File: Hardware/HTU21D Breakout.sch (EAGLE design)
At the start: 13 parts, among them U1 HTU21D

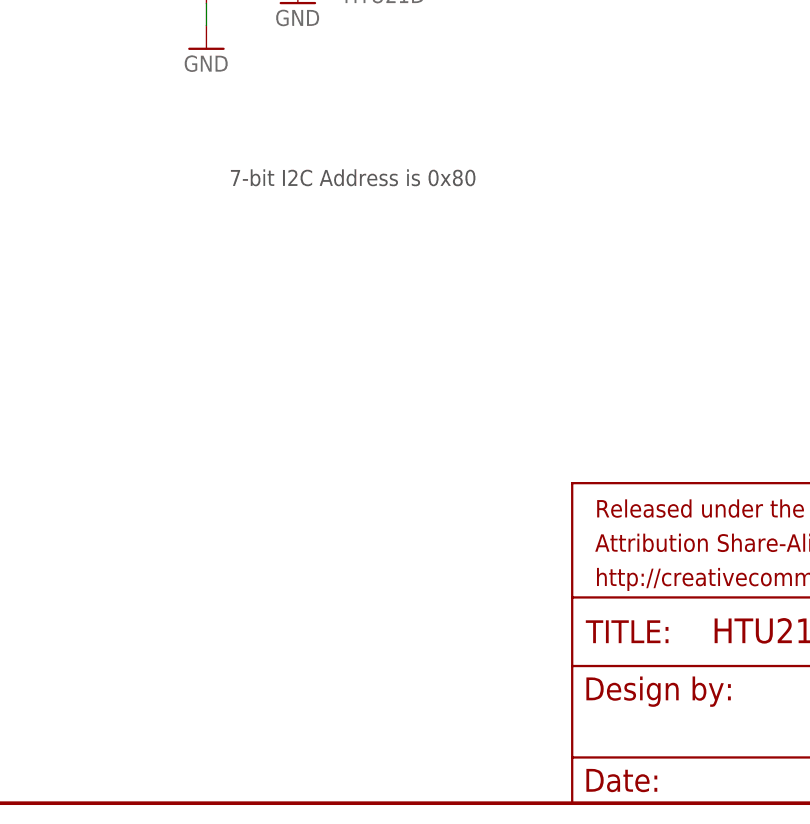
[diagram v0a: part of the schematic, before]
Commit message: Re-routing post review with engineering recommendations.
Moved to 0603 footprints. Removed ground planes to align with datasheet
thermal recommendations. Added OSHW logo. Updated frame to CC 3.0. Added
revision code to bottom copper.
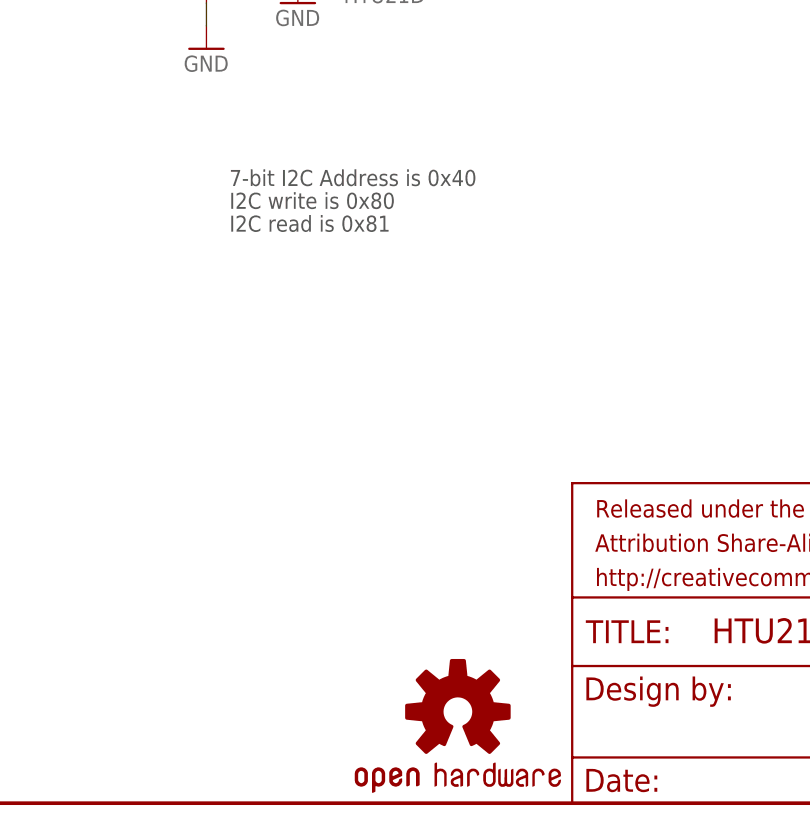
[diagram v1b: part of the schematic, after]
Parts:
- added LOGO2: OSHW-LOGOS, SparkFun-Aesthetics:OSHW-LOGOS
- C1: device SparkFun:CAP0402-CAP -> SparkFun:CAP0603-CAP
- R1, R2: device SparkFun:RESISTOR0402-RES -> SparkFun:RESISTOR0603-RES
- renumbered FRAME1 to FRAME2
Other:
- note added: "7-bit I2C Address is 0x40"
- note added: "I2C read is 0x81"
- note added: "I2C write is 0x80"
- note removed: "7-bit I2C Address is 0x80"
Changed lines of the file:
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@@
 <?xml version="1.0" encoding="utf-8"?>
 <!DOCTYPE eagle SYSTEM "eagle.dtd">
-<eagle version="6.5.0">
+<eagle version="6.4">
 <drawing>
 <settings>
@@
 </classes>
 <parts>
-<part name="FRAME1" library="SparkFun-Aesthetics" deviceset="FRAME-LETTER" device=""/>
 <part name="LOGO1" library="SparkFun" deviceset="LOGO-SFE" device="SK"/>
-<part name="C1" library="SparkFun" deviceset="CAP" device="0402-CAP" value="0.1uF"/>
-<part name="R1" library="SparkFun" deviceset="RESISTOR" device="0402-RES" value="4.7k"/>
-<part name="R2" library="SparkFun" deviceset="RESISTOR" device="0402-RES" value="4.7k"/>
+<part name="C1" library="SparkFun" deviceset="CAP" device="0603-CAP" value="0.1uF"/>
+<part name="R1" library="SparkFun" deviceset="RESISTOR" device="0603-RES" value="4.7k"/>
+<part name="R2" library="SparkFun" deviceset="RESISTOR" device="0603-RES" value="4.7k"/>
 <part name="GND1" library="SparkFun" deviceset="GND" device=""/>
 <part name="P+1" library="SparkFun" deviceset="VCC" device="" value="3.3V"/>
@@
 <part name="U1" library="SparkFun-Sensors" deviceset="HTU21D" device="SMD" value="HTU21D"/>
 <part name="JP5" library="SparkFun-Connectors" deviceset="M04" device="PTH"/>
+<part name="LOGO2" library="SparkFun-Aesthetics" deviceset="OSHW-LOGO" device="S"/>
+<part name="FRAME2" library="SparkFun-Aesthetics" deviceset="FRAME-LETTER" device=""/>
 </parts>
 <sheets>
@@
 <text x="167.64" y="114.3" size="1.778" layer="97">TO DISABLE I2C PULLUP RESISTORS</text>
 <text x="45.72" y="121.92" size="1.778" layer="97">VCC RANGE: 1.5V TO 3.6V</text>
-<text x="109.22" y="68.58" size="1.778" layer="97">7-bit I2C Address is 0x80</text>
+<text x="109.22" y="68.58" size="1.778" layer="97">7-bit I2C Address is 0x40</text>
+<text x="109.22" y="66.04" size="1.778" layer="97">I2C write is 0x80</text>
+<text x="109.22" y="63.5" size="1.778" layer="97">I2C read is 0x81</text>
 </plain>
 <instances>
-<instance part="FRAME1" gate="G$1" x="0" y="0"/>
-<instance part="FRAME1" gate="G$2" x="147.32" y="0"/>
 <instance part="LOGO1" gate="G$1" x="226.06" y="27.94"/>
 <instance part="C1" gate="G$1" x="106.68" y="91.44"/>
@@
 <instance part="U1" gate="U$1" x="129.54" y="96.52"/>
 <instance part="JP5" gate="G$1" x="55.88" y="104.14"/>
+<instance part="LOGO2" gate="G$1" x="134.62" y="10.16"/>
+<instance part="FRAME2" gate="G$1" x="0" y="0"/>
+<instance part="FRAME2" gate="G$2" x="147.32" y="0"/>
 </instances>
 <busses>

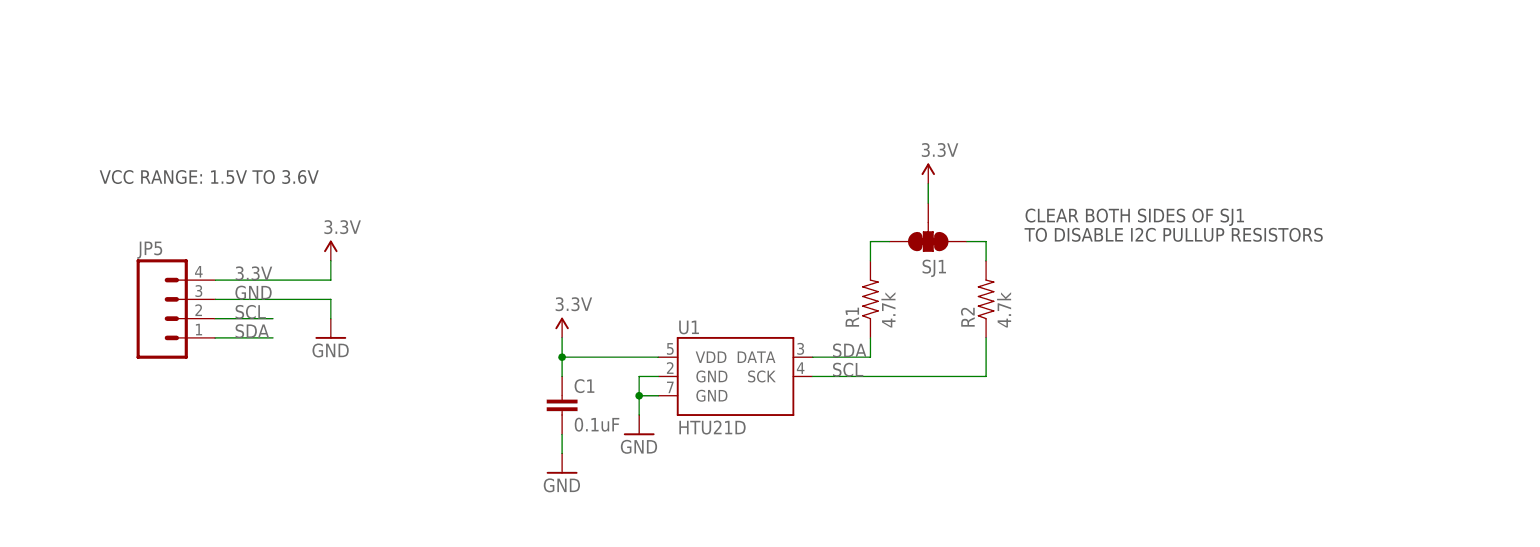
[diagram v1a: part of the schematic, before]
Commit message: Added flags on data lines to schematic.
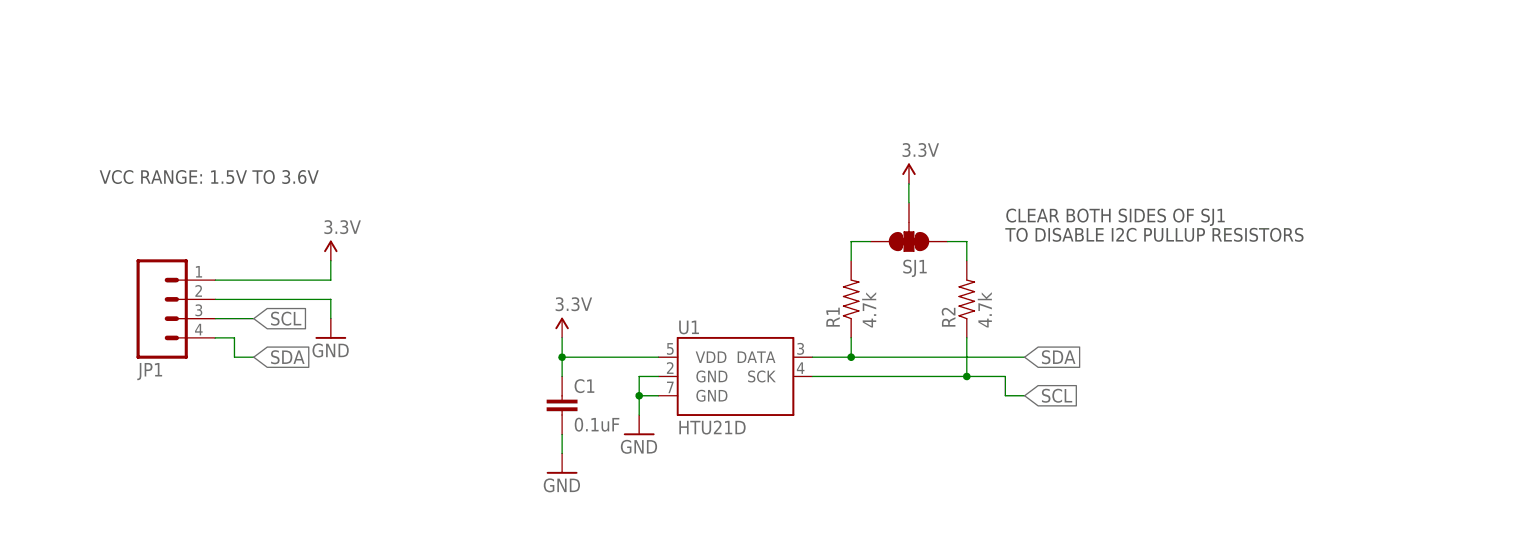
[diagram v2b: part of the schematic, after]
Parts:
- removed JP5: (no value), SparkFun-Connectors:M04PTH
- added JP1: (no value), SparkFun-Connectors:M04PTH
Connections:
- net 3.3V: now also JP1.1; no longer JP5.4
- net GND: now also JP1.2; no longer JP5.3
- net SCL: now also JP1.3; no longer JP5.2
- net SDA: now also JP1.4; no longer JP5.1
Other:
- moved on the sheet: R1, R2, SJ1

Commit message: Corrected a reversed the footprint.
Arg! I forgot to invert the footprint. Corrected.
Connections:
- net SCL: now also JP1.4; no longer JP1.3
- net SDA: now also JP1.3; no longer JP1.4
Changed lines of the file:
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@@
 <?xml version="1.0" encoding="utf-8"?>
 <!DOCTYPE eagle SYSTEM "eagle.dtd">
-<eagle version="6.4">
+<eagle version="6.5.0">
 <drawing>
 <settings>
@@
 </segment>
 <segment>
-<label x="66.04" y="104.14" size="1.778" layer="95" xref="yes"/>
-<pinref part="JP1" gate="G$1" pin="3"/>
-<wire x1="60.96" y1="104.14" x2="66.04" y2="104.14" width="0.1524" layer="91"/>
+<label x="66.04" y="99.06" size="1.778" layer="95" xref="yes"/>
+<pinref part="JP1" gate="G$1" pin="4"/>
+<wire x1="60.96" y1="101.6" x2="63.5" y2="101.6" width="0.1524" layer="91"/>
+<wire x1="63.5" y1="101.6" x2="63.5" y2="99.06" width="0.1524" layer="91"/>
+<wire x1="66.04" y1="99.06" x2="63.5" y2="99.06" width="0.1524" layer="91"/>
 </segment>
 </net>
@@
 </segment>
 <segment>
-<label x="66.04" y="99.06" size="1.778" layer="95" xref="yes"/>
-<wire x1="60.96" y1="101.6" x2="63.5" y2="101.6" width="0.1524" layer="91"/>
-<wire x1="63.5" y1="101.6" x2="63.5" y2="99.06" width="0.1524" layer="91"/>
-<wire x1="63.5" y1="99.06" x2="66.04" y2="99.06" width="0.1524" layer="91"/>
-<pinref part="JP1" gate="G$1" pin="4"/>
+<label x="66.04" y="104.14" size="1.778" layer="95" xref="yes"/>
+<pinref part="JP1" gate="G$1" pin="3"/>
+<wire x1="60.96" y1="104.14" x2="66.04" y2="104.14" width="0.1524" layer="91"/>
 </segment>
 </net>
